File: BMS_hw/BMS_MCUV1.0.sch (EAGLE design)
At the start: 48 parts, among them IC2 SST25VF020B804ISA, J1 22-27-2051-05, J2 22-27-2051-05, J3 22-27-2041-04, J4 22-27-2051-05, Q2 32.768kHz, U1 NCP1117LP-PG, X1 87758-2016

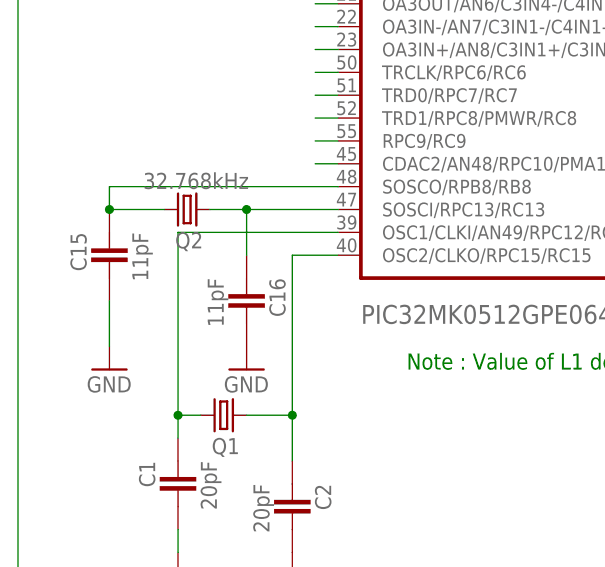
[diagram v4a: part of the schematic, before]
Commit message: secondary osc removed
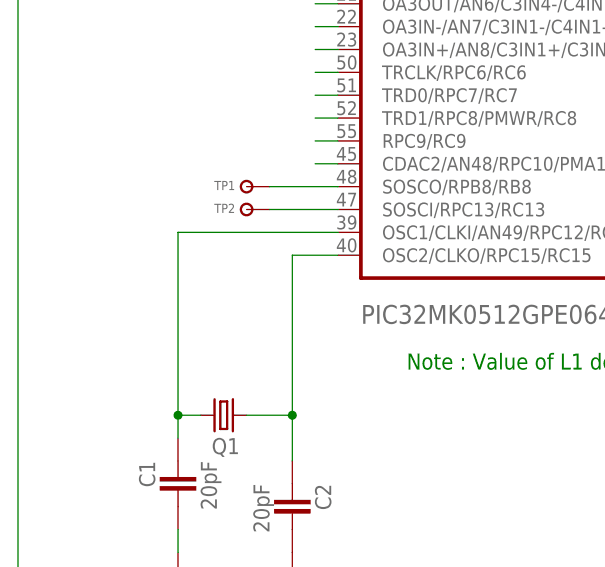
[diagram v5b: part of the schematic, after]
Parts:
- removed C15, C16: 11pF, ipc-7351-capacitor:CAPACITOR_0603
- removed Q2: 32.768kHz, adafruit:CRYSTALCTS406
- added TP1, TP2: TP-SMD60, simpa:TP-SMD60
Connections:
- removed net N$17: C16.1, MCU2.SOSCI/RPC13/RC13, Q2.1
- new net N$5: MCU2.SOSCO/RPB8/RB8, TP1.P$1
- net GND: no longer C15.2, C16.2
- net N$16: now also MCU2.SOSCI/RPC13/RC13, TP2.P$1; no longer C15.1, MCU2.SOSCO/RPB8/RB8, Q2.2
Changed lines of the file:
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@@
 <setting verticaltext="up"/>
 </settings>
-<grid distance="0.1" unitdist="inch" unit="mil" style="lines" multiple="1" display="no" altdistance="0.01" altunitdist="inch" altunit="mil"/>
+<grid distance="0.1" unitdist="inch" unit="inch" style="lines" multiple="1" display="no" altdistance="0.01" altunitdist="inch" altunit="inch"/>
 <layers>
 <layer number="1" name="Top" color="4" fill="1" visible="no" active="no"/>
@@
 <part name="GND17" library="supply1" library_urn="urn:adsk.eagle:library:371" deviceset="GND" device=""/>
 <part name="GND18" library="supply1" library_urn="urn:adsk.eagle:library:371" deviceset="GND" device=""/>
-<part name="Q2" library="adafruit" deviceset="CRYSTAL" device="CTS406" value="32.768kHz"/>
-<part name="C15" library="ipc-7351-capacitor" deviceset="CAPACITOR_" device="0603" value="11pF"/>
-<part name="C16" library="ipc-7351-capacitor" deviceset="CAPACITOR_" device="0603" value="11pF"/>
-<part name="GND19" library="supply1" library_urn="urn:adsk.eagle:library:371" deviceset="GND" device=""/>
-<part name="GND20" library="supply1" library_urn="urn:adsk.eagle:library:371" deviceset="GND" device=""/>
 <part name="J1" library="con-molex" library_urn="urn:adsk.eagle:library:165" deviceset="22-?-05" device="27-2051"/>
 <part name="R8" library="ipc-7351-resistor" deviceset="RESISTOR_" device="0805" value="2.2k"/>
@@
 <part name="GND4" library="supply1" library_urn="urn:adsk.eagle:library:371" deviceset="GND" device=""/>
 <part name="GND5" library="supply1" library_urn="urn:adsk.eagle:library:371" deviceset="GND" device=""/>
+<part name="TP1" library="simpa" deviceset="TP" device="-SMD60"/>
+<part name="TP2" library="simpa" deviceset="TP" device="-SMD60"/>
 </parts>
 <sheets>
@@
 <instance part="GND17" gate="1" x="279.4" y="149.86"/>
 <instance part="GND18" gate="1" x="220.98" y="147.32"/>
-<instance part="Q2" gate="G$1" x="28.956" y="58.42" smashed="yes" rot="R180">
-<attribute name="NAME" x="30.734" y="55.88" size="1.778" layer="95" rot="R180"/>
-<attribute name="VALUE" x="35.814" y="62.484" size="1.778" layer="96" rot="R180"/>
-</instance>
-<instance part="C15" gate="G$1" x="20.32" y="53.34" rot="MR270"/>
-<instance part="C16" gate="G$1" x="35.56" y="48.26" rot="R270"/>
-<instance part="GND19" gate="1" x="20.32" y="40.64"/>
-<instance part="GND20" gate="1" x="35.56" y="40.64"/>
 <instance part="J1" gate="-1" x="332.74" y="190.5"/>
 <instance part="J1" gate="-2" x="332.74" y="180.34"/>
@@
 <instance part="GND4" gate="1" x="266.7" y="182.88"/>
 <instance part="GND5" gate="1" x="231.14" y="182.88"/>
+<instance part="TP1" gate="G$1" x="35.56" y="60.96" rot="R180"/>
+<instance part="TP2" gate="G$1" x="35.56" y="58.42" rot="R180"/>
 </instances>
 <busses>
@@
 <wire x1="223.52" y1="152.4" x2="220.98" y2="152.4" width="0.1524" layer="91"/>
 <wire x1="220.98" y1="152.4" x2="220.98" y2="149.86" width="0.1524" layer="91"/>
-</segment>
-<segment>
-<pinref part="C15" gate="G$1" pin="2"/>
-<pinref part="GND19" gate="1" pin="GND"/>
-<wire x1="20.32" y1="48.26" x2="20.32" y2="43.18" width="0.1524" layer="91"/>
-</segment>
-<segment>
-<pinref part="C16" gate="G$1" pin="2"/>
-<pinref part="GND20" gate="1" pin="GND"/>
 </segment>
 <segment>
@@
 </segment>
 </net>
-<net name="N$16" class="0">
-<segment>
-<pinref part="C15" gate="G$1" pin="1"/>
-<pinref part="Q2" gate="G$1" pin="2"/>
-<wire x1="20.32" y1="58.42" x2="26.416" y2="58.42" width="0.1524" layer="91"/>
-<junction x="20.32" y="58.42"/>
-<pinref part="MCU2" gate="G$1" pin="SOSCO/RPB8/RB8"/>
-<wire x1="20.32" y1="60.96" x2="20.32" y2="58.42" width="0.1524" layer="91"/>
-<wire x1="45.72" y1="60.96" x2="20.32" y2="60.96" width="0.1524" layer="91"/>
-</segment>
-</net>
 <net name="VDD" class="0">
 <segment>
@@
 </segment>
 </net>
-<net name="N$17" class="0">
-<segment>
-<pinref part="Q2" gate="G$1" pin="1"/>
+<net name="N$5" class="0">
+<segment>
+<pinref part="TP1" gate="G$1" pin="P$1"/>
+<pinref part="MCU2" gate="G$1" pin="SOSCO/RPB8/RB8"/>
+<wire x1="38.1" y1="60.96" x2="45.72" y2="60.96" width="0.1524" layer="91"/>
+</segment>
+</net>
+<net name="N$16" class="0">
+<segment>
+<pinref part="TP2" gate="G$1" pin="P$1"/>
 <pinref part="MCU2" gate="G$1" pin="SOSCI/RPC13/RC13"/>
-<wire x1="31.496" y1="58.42" x2="35.56" y2="58.42" width="0.1524" layer="91"/>
-<pinref part="C16" gate="G$1" pin="1"/>
-<wire x1="35.56" y1="58.42" x2="45.72" y2="58.42" width="0.1524" layer="91"/>
-<wire x1="35.56" y1="53.34" x2="35.56" y2="58.42" width="0.1524" layer="91"/>
-<junction x="35.56" y="58.42"/>
-</segment>
-</net>
+<wire x1="38.1" y1="58.42" x2="45.72" y2="58.42" width="0.1524" layer="91"/>
+</segment>
+</net>

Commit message: placment 80% done
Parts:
- added X2, X3: (no value), con-molex:KK-156-10
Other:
- note added: "Greenfuel Energy Solutions Pvt. Ltd."
